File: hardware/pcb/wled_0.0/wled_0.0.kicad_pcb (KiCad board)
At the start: 2 copper layers, 26 x 40.5 mm, 13 parts, among them J1 Conn_01x02_Female, J2 Conn_01x03_Female, Q1 BSS138, U1 AMS1117-3.3, U2 ESP-12

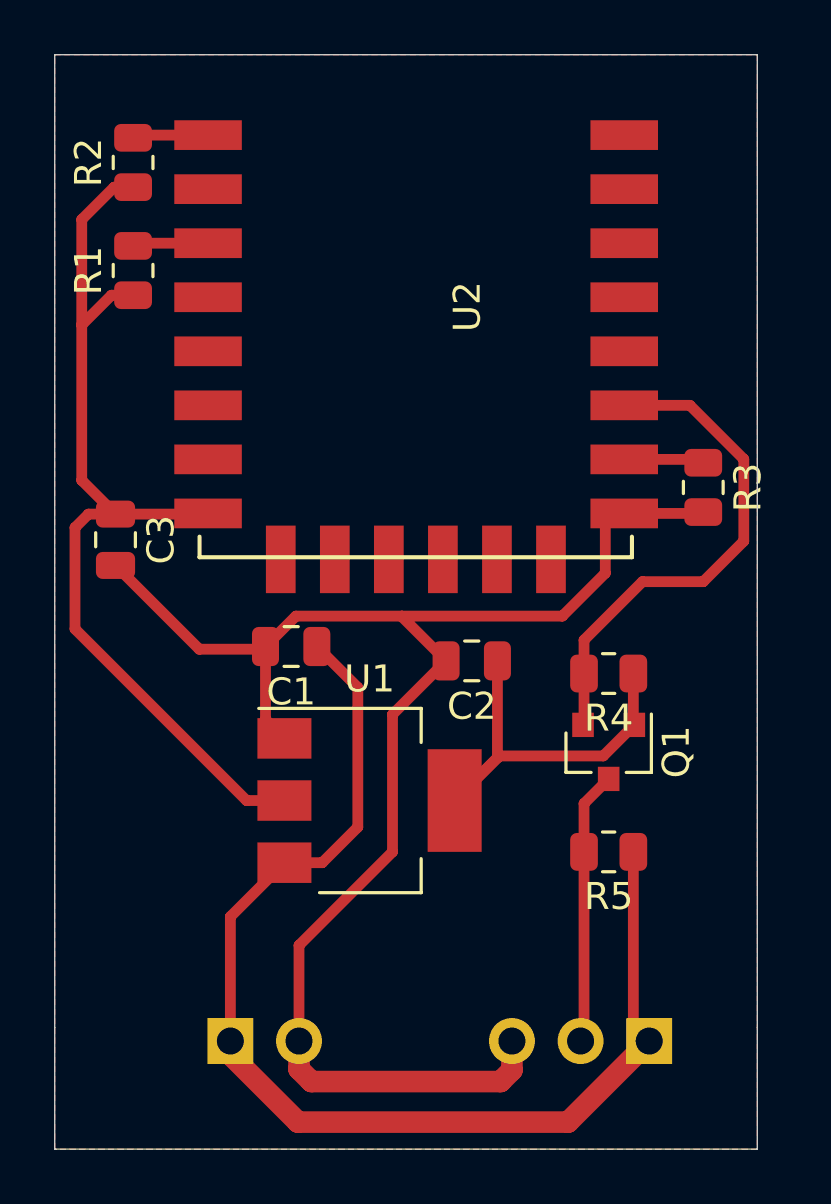
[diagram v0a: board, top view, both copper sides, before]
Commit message: правки в схеие и плате:
- заменил значения резисторов с 4к7 на 10к
- перенес некоторые дорожки дальше от края, увеличил размер площадок под сверловку
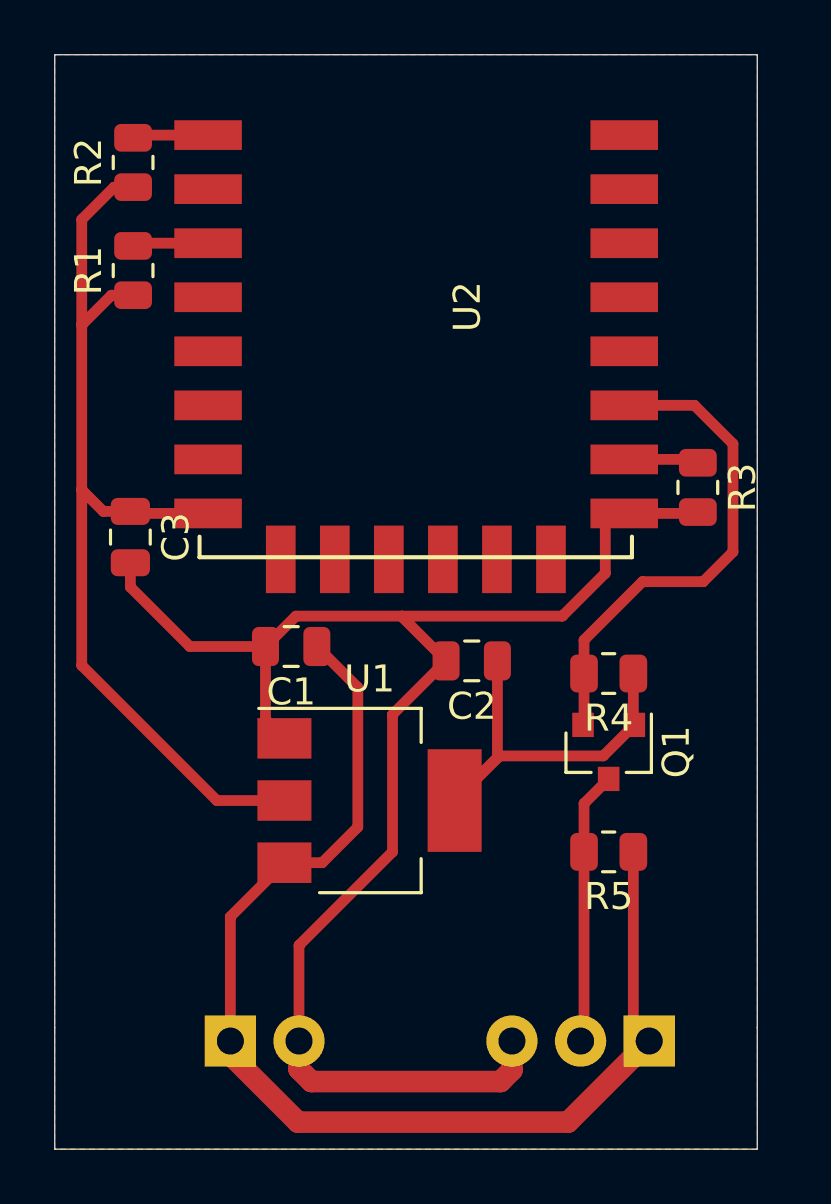
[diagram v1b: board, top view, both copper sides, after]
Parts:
- moved C3 0.56 mm to (22.8, 49.9)
- moved R3 0.20 mm to (43.8, 48.0)
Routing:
- net Net-(C2-Pad1): track 51.9 -> 52.6 mm
